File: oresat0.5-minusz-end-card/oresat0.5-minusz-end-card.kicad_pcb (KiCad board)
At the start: 4 copper layers, 99.8 x 94.6 mm, 36 parts, among them J1 J-SAMTEC-TFM-120-01-L-D-RA, J2 U.FL-R-SMT-1, J3 Harwin M55-7101242R, J4 UHF Feed, J5 Harwin M55-7101242R, J6 L-Band Feed

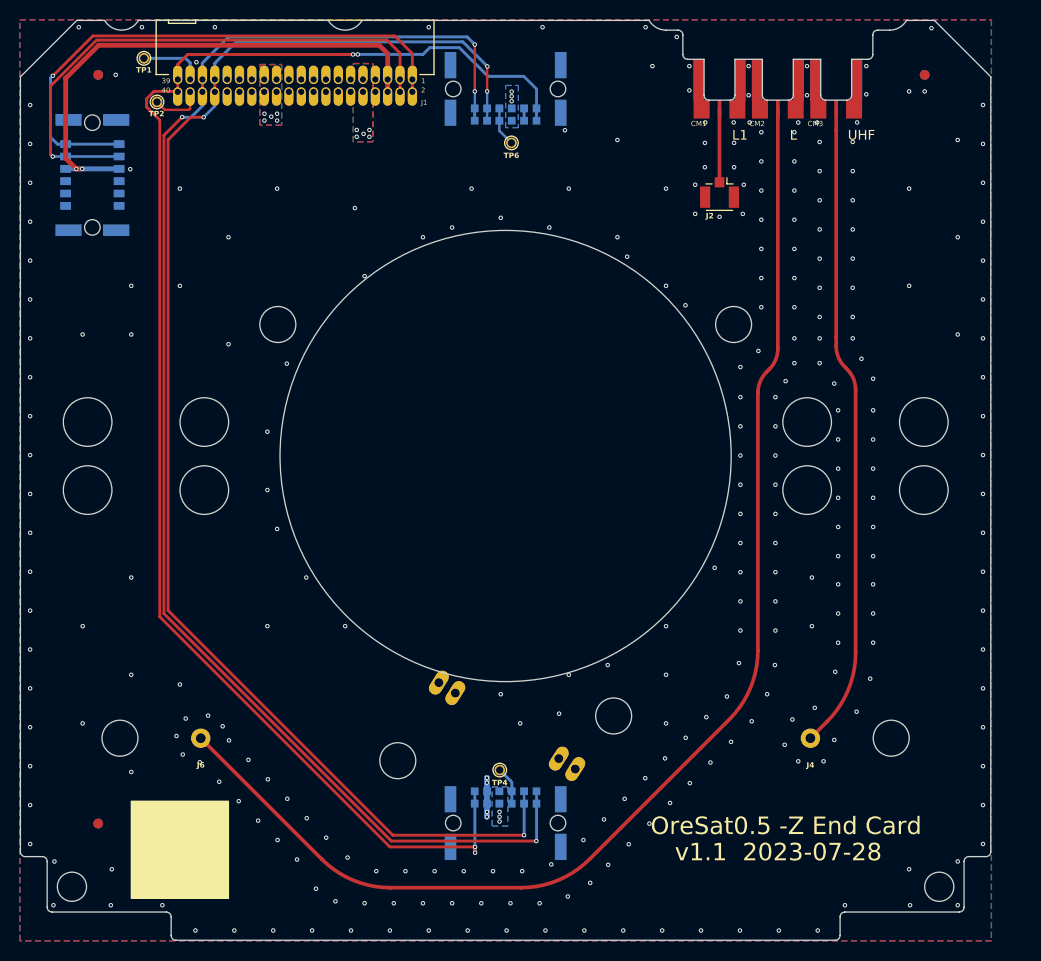
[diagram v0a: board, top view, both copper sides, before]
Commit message: Fixed up OreSat0.5 -Z end card: Added hole for U.FL connector to get to GPS antnena, fixed library paths which seemed broken, replaced older EAGLE files too, fixed schematic/board disconnect with ref designators, cleaned up ERCs and DRCs.
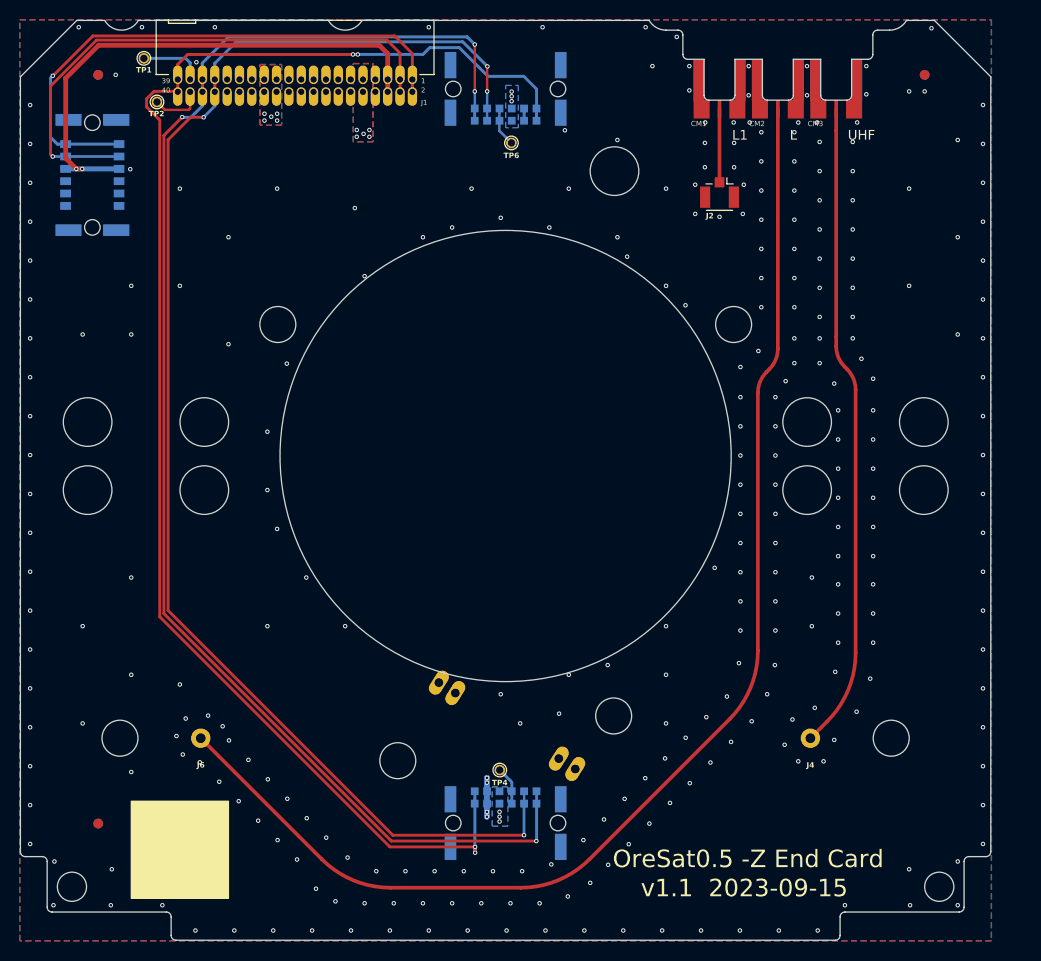
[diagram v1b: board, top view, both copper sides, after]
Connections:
- net /CONNECTORS/+X_AUX renamed /-X_AUX
- net /CONNECTORS/-X_AUX renamed /+X_AUX
- net /CONNECTORS/C3-UART-RX renamed /C3-UART-RX
- net /CONNECTORS/C3-UART-TX renamed /C3-UART-TX
- net /CONNECTORS/CAN1_H renamed /CAN1_H
- net /CONNECTORS/CAN1_L renamed /CAN1_L
- net /CONNECTORS/MAG-POWER renamed /MAG-POWER
- net /CONNECTORS/MAG-SCL renamed /MAG-SCL
- net /CONNECTORS/MAG-SDA renamed /MAG-SDA
- net /CONNECTORS/TURNSTILE-DEPLOY renamed /TURNSTILE-DEPLOY
- net /CONNECTORS/~{SD} renamed /~{SD}
- net /L BAND/LBAND renamed /LBAND
- net /L1 BAND/L1BAND renamed /L1BAND
- net /UHF/UHF renamed /UHF
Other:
- board text added: "v1.1 2023-09-15"
- board text removed: "v1.1 2023-07-28"

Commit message: Moves antenna connection from large vias to slots so we don't need an a lead on the 1/4 inch tape measure antennas.
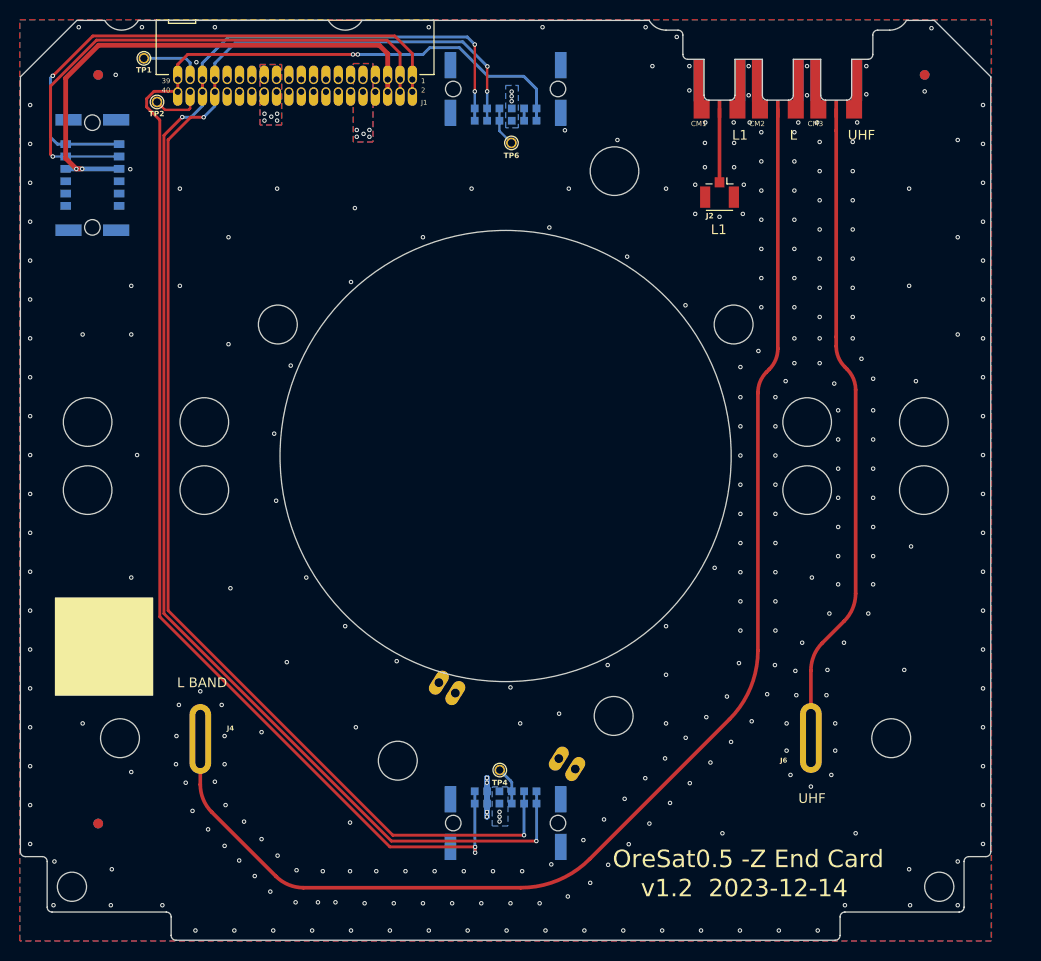
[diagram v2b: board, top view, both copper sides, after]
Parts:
- J4: value UHF Feed -> ~; footprint Connector_Pin:Pin_D1.0mm_L10.0mm -> oresat-misc:tape-measure-slot-antenna
- J6: value L-Band Feed -> ~; footprint Connector_Pin:Pin_D1.0mm_L10.0mm -> oresat-misc:tape-measure-slot-antenna
- moved J4 62.8 mm to (117.1, 131.6), turned to 90 degrees
- moved J6 62.8 mm to (179.9, 131.5), turned to 90 degrees
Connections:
- J4 pad 1: /UHF -> /LBAND
- J6 pad 1: /LBAND -> /UHF
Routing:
- net /LBAND: track 131.0 -> 134.9 mm
- net GND: vias 300 -> 308
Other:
- board text added: "L BAND"
- board text added: "v1.2 2023-12-14"
- board text removed: "v1.1 2023-09-15"

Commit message: Updated solar module connector positions
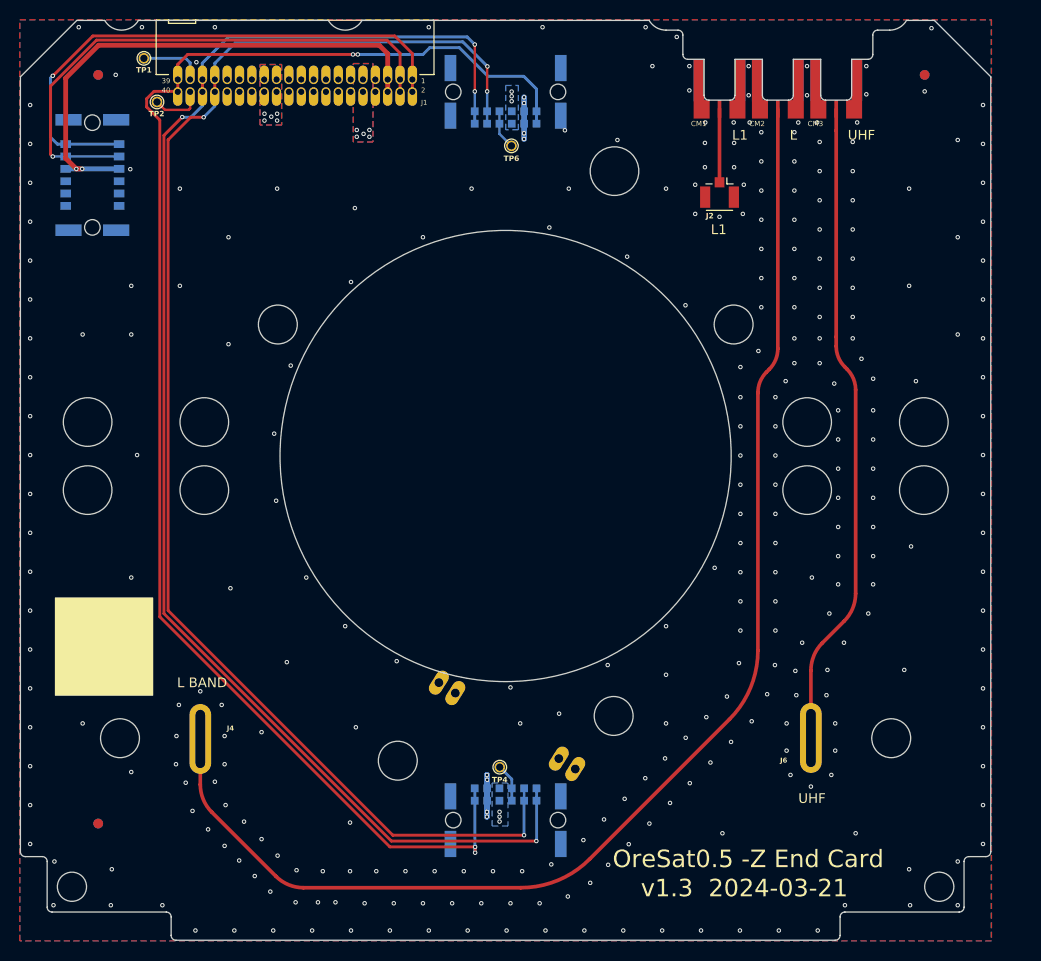
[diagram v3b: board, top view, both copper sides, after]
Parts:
- moved TP6 0.30 mm to (149.1, 70.6)
- moved J5 0.30 mm to (148.5, 65.0)
- moved J3 0.30 mm to (148.5, 139.9)
- moved TP4 0.30 mm to (147.9, 134.5)
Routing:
- net GND: track 5.27 -> 8.60 mm, vias 308 -> 312
- net /~{SD}: track 154.3 -> 155.2 mm
- net /CAN1_L: track 149.4 -> 150.0 mm
- net /CAN1_H: track 145.4 -> 146.0 mm
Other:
- board text added: "v1.3 2024-03-21"
- board text removed: "v1.2 2023-12-14"

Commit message: Updated date and unecessary polish on planes, including fillets and just more planes with more vias.
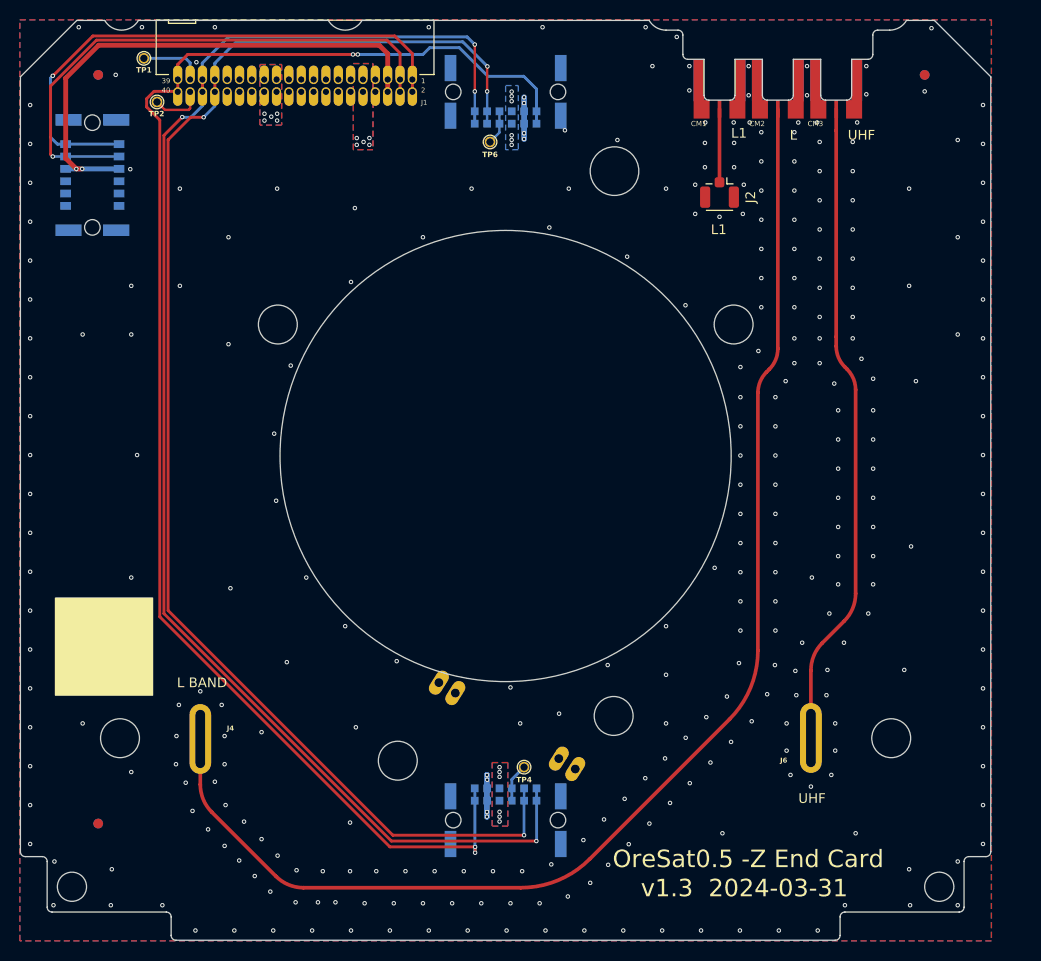
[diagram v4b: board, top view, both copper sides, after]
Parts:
- removed REF** (x8): MountingHole_5mm, MountingHole:MountingHole_5mm
- moved TP4 2.50 mm to (150.4, 134.5)
- moved TP6 2.24 mm to (146.9, 70.2)
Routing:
- net /+X_AUX: track 4.06 -> 3.55 mm
- net VBUS: vias 11 -> 17
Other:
- board text added: "v1.3 2024-03-31"
- board text removed: "v1.3 2024-03-21"

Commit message: Added M2 fastener holes back into the -Z end card. Rev'd to v1.4.
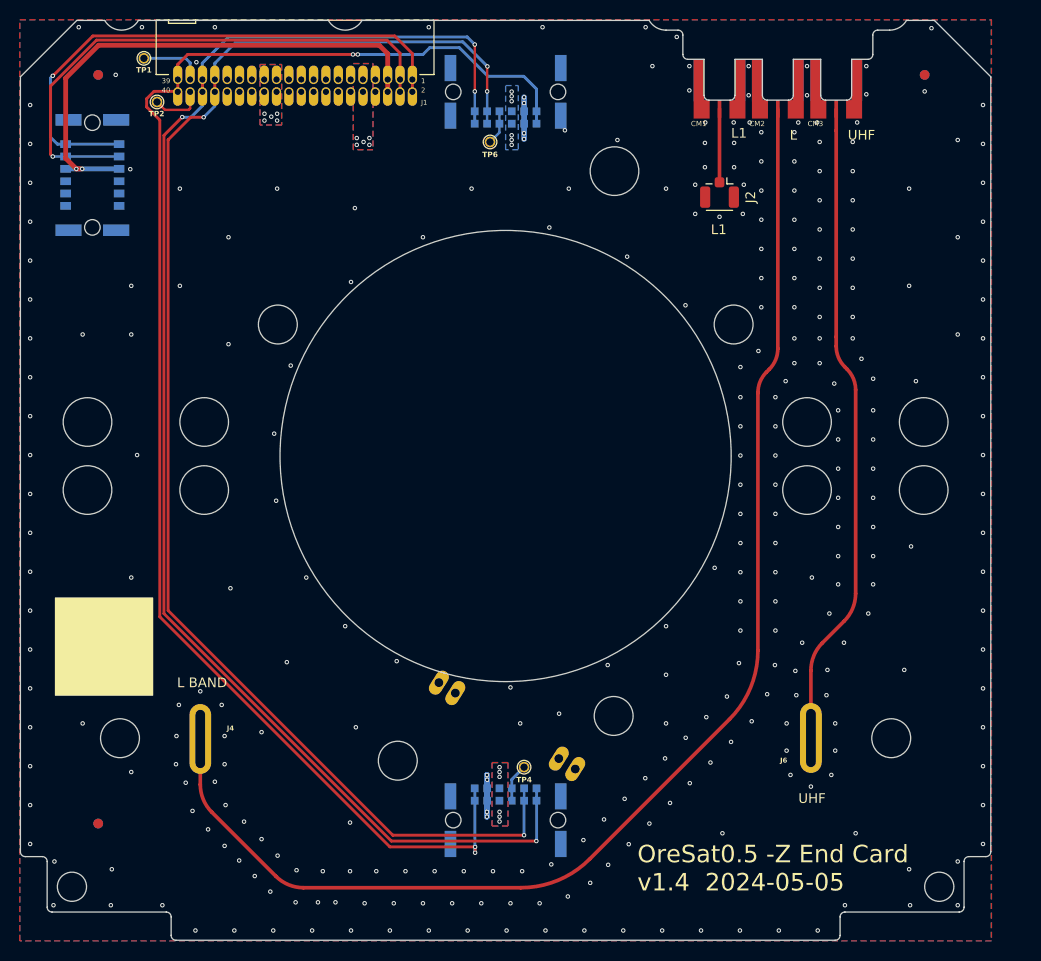
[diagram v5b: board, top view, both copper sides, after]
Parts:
- added H101: MountingHole, MountingHole:MountingHole_5mm, F.Cu at (105.5, 99.0)
- added H102: MountingHole, MountingHole:MountingHole_5mm, F.Cu at (117.5, 99.0)
- added H103: MountingHole, MountingHole:MountingHole_5mm, F.Cu at (105.5, 106.0)
- added H104: MountingHole, MountingHole:MountingHole_5mm, F.Cu at (117.5, 106.0)
- added H105: MountingHole, MountingHole:MountingHole_5mm, F.Cu at (179.5, 99.0)
- added H106: MountingHole, MountingHole:MountingHole_5mm, F.Cu at (179.5, 106.0)
- added H107: MountingHole, MountingHole:MountingHole_5mm, F.Cu at (191.5, 99.0)
- added H108: MountingHole, MountingHole:MountingHole_5mm, F.Cu at (191.5, 106.0)
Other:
- board text added: "OreSat0.5 -Z End Card ${REVISION} ${ISSUE_DATE}"
- board text removed: "OreSat0.5 -Z End Card"
- board text removed: "v1.3 2024-03-31"

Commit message: initial mounting holes changes for new deployer
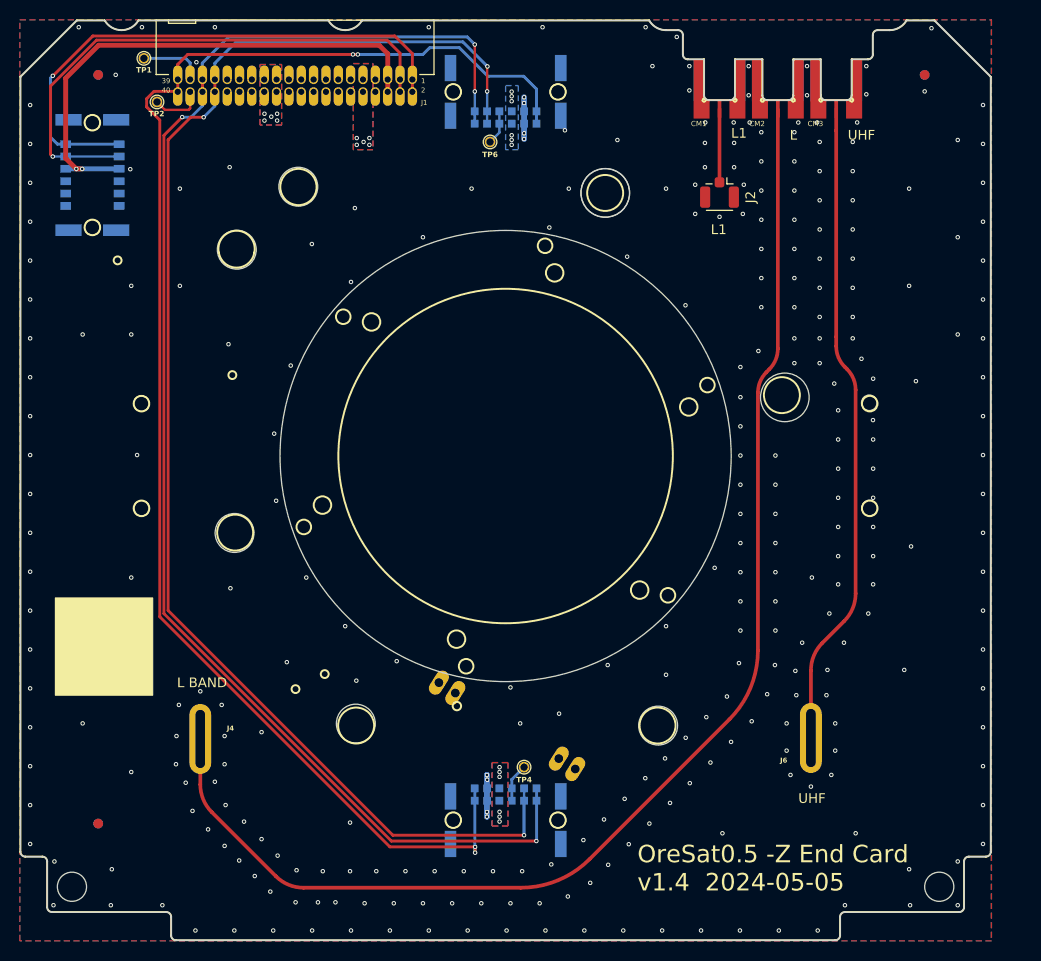
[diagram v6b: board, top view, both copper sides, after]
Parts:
- removed H101, H102, H103, H104, H105, H106: MountingHole, MountingHole:MountingHole_5mm
- removed HW1, HW4, HW5: M2-Press-Fit-Nut, oresat-misc:M2-Press-Fit-Nut
- added ?: , , F.Cu at (111.1, 107.9)
- added ?: , , F.Cu at (120.6, 110.4)
- added ?: , , F.Cu at (111.0, 97.1)
- added ?: , , F.Cu at (127.2, 74.8)
- added ?: , , F.Cu at (185.9, 97.0)
- added ?: , , F.Cu at (185.9, 107.8)
- moved H108 44.8 mm to (158.8, 75.4)
- moved H107 14.5 mm to (177.2, 96.5)
- moved HW6 8.78 mm to (120.9, 81.3)
- moved HW3 5.76 mm to (133.1, 130.0)
- moved HW2 4.68 mm to (164.2, 130.2)
- turned R1 to 57.65 degrees
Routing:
- net GND: vias 312 -> 308

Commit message: Revert "initial mounting holes changes for new deployer" -- oops, wrong end card.
This reverts commit 281d3ddd2ce643add95357c75bebd497bf0c76a9.
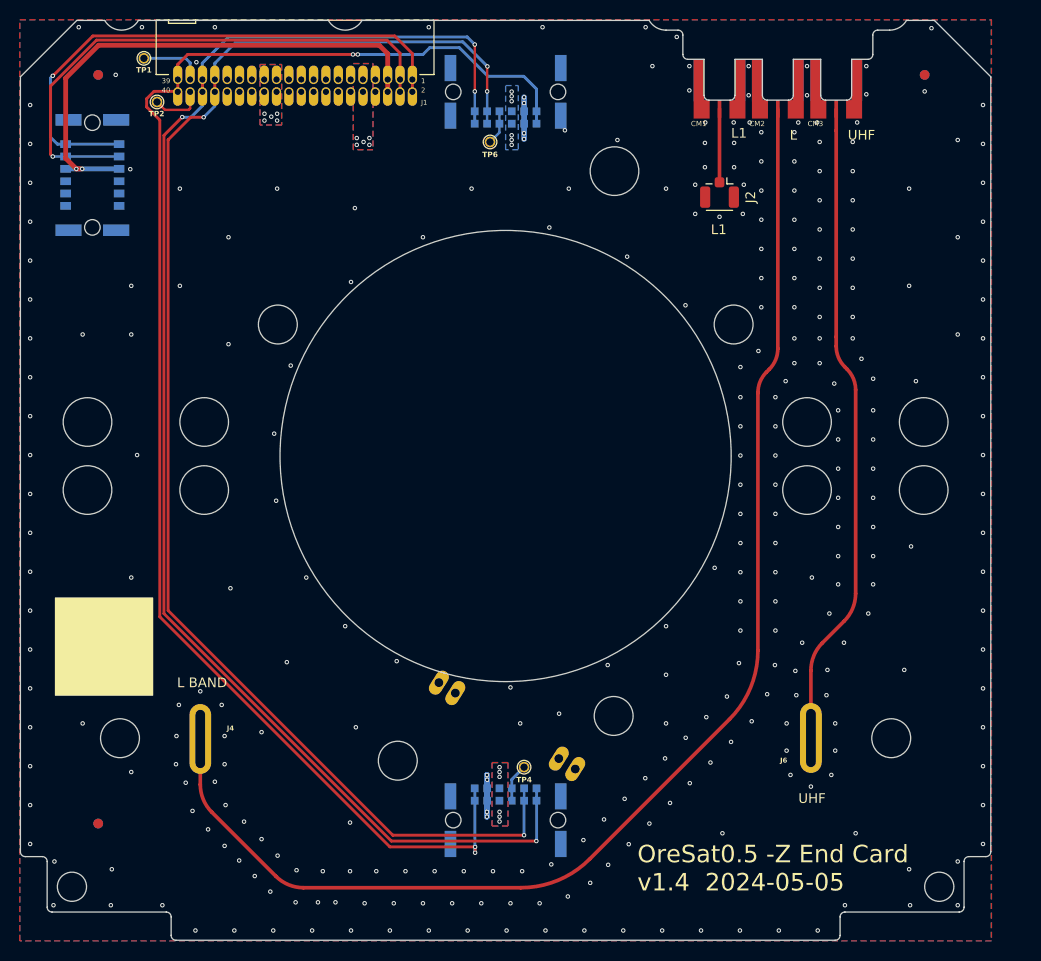
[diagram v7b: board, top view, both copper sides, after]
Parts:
- removed ? (x6): , 
- added H101: MountingHole, MountingHole:MountingHole_5mm, F.Cu at (105.5, 99.0)
- added H102: MountingHole, MountingHole:MountingHole_5mm, F.Cu at (117.5, 99.0)
- added H103: MountingHole, MountingHole:MountingHole_5mm, F.Cu at (105.5, 106.0)
- added H104: MountingHole, MountingHole:MountingHole_5mm, F.Cu at (117.5, 106.0)
- added H105: MountingHole, MountingHole:MountingHole_5mm, F.Cu at (179.5, 99.0)
- added H106: MountingHole, MountingHole:MountingHole_5mm, F.Cu at (179.5, 106.0)
- added HW1: M2-Press-Fit-Nut, oresat-misc:M2-Press-Fit-Nut, B.Cu at (188.2, 131.5)
- added HW4: M2-Press-Fit-Nut, oresat-misc:M2-Press-Fit-Nut, B.Cu at (108.8, 131.5)
- added HW5: M2-Press-Fit-Nut, oresat-misc:M2-Press-Fit-Nut, B.Cu at (172.0, 89.0)
- moved H108 44.8 mm to (191.5, 106.0)
- moved H107 14.5 mm to (191.5, 99.0)
- moved HW6 8.78 mm to (125.1, 89.0)
- moved HW3 5.76 mm to (137.4, 133.8)
- moved HW2 4.68 mm to (159.6, 129.2)
- turned R1 to -122.35 degrees
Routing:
- net GND: vias 308 -> 312
